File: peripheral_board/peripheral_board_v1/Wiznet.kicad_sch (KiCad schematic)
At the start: 27 parts, among them U4 W5500, Y2 25MHZ

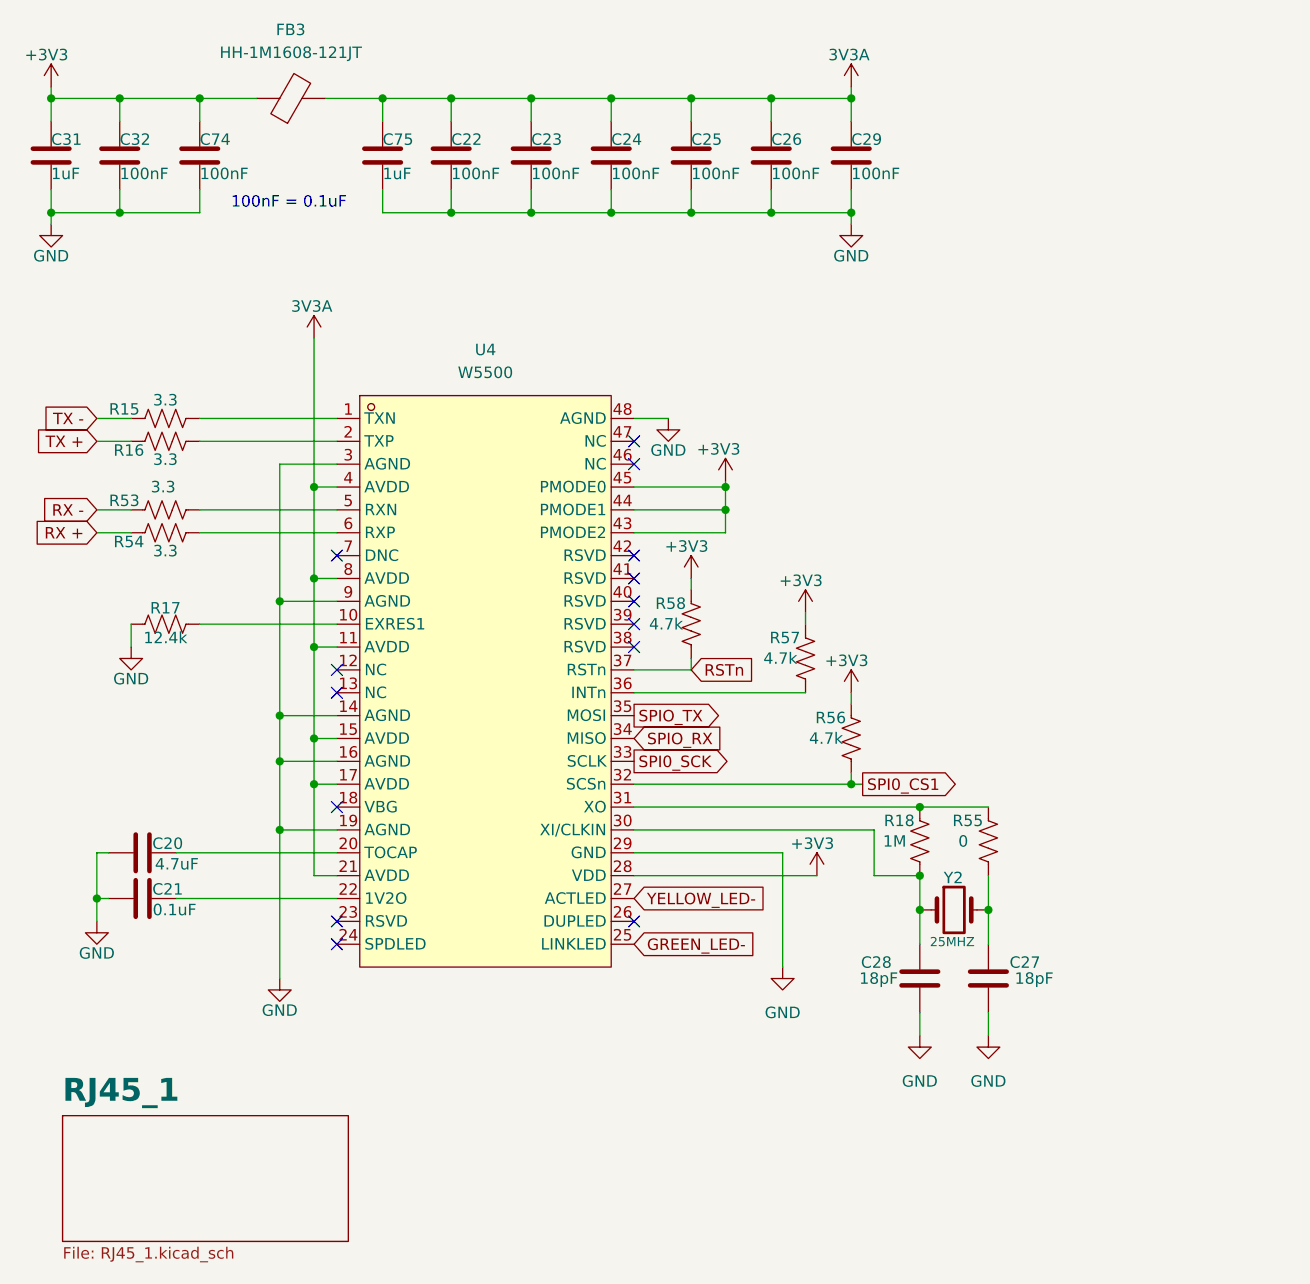
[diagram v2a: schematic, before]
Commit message: Update to the PCB
#Changes made so far

## Wiznet
* Changed the Wiznet layout to match that of their development board
* Restructured the RJ45 connections
    * *Looked over the RJ45 still a unsure*
    * Added in 2 differnt versions of Ethernt Connections. The one that shows the magnetics might be used for the Ethernet switch.
* Removed the Single Bus Buffer gate with 3-state output to match the dev board

## Raspberry Pi
* Moved to USB type C from micro USB for debugging.
* Changed the GPIO pins to match the Wiznet dev board.
* Brought in breakout pins for the rest of the GPIO.
* Cleaned up the Schematic to make it more clean.

## Ethernet Switch
* Changed the crystal to be the same as the Wiznet and to have the correct load caps
* Looking at the design check list to help get moving forward, need to relook at power distribution.
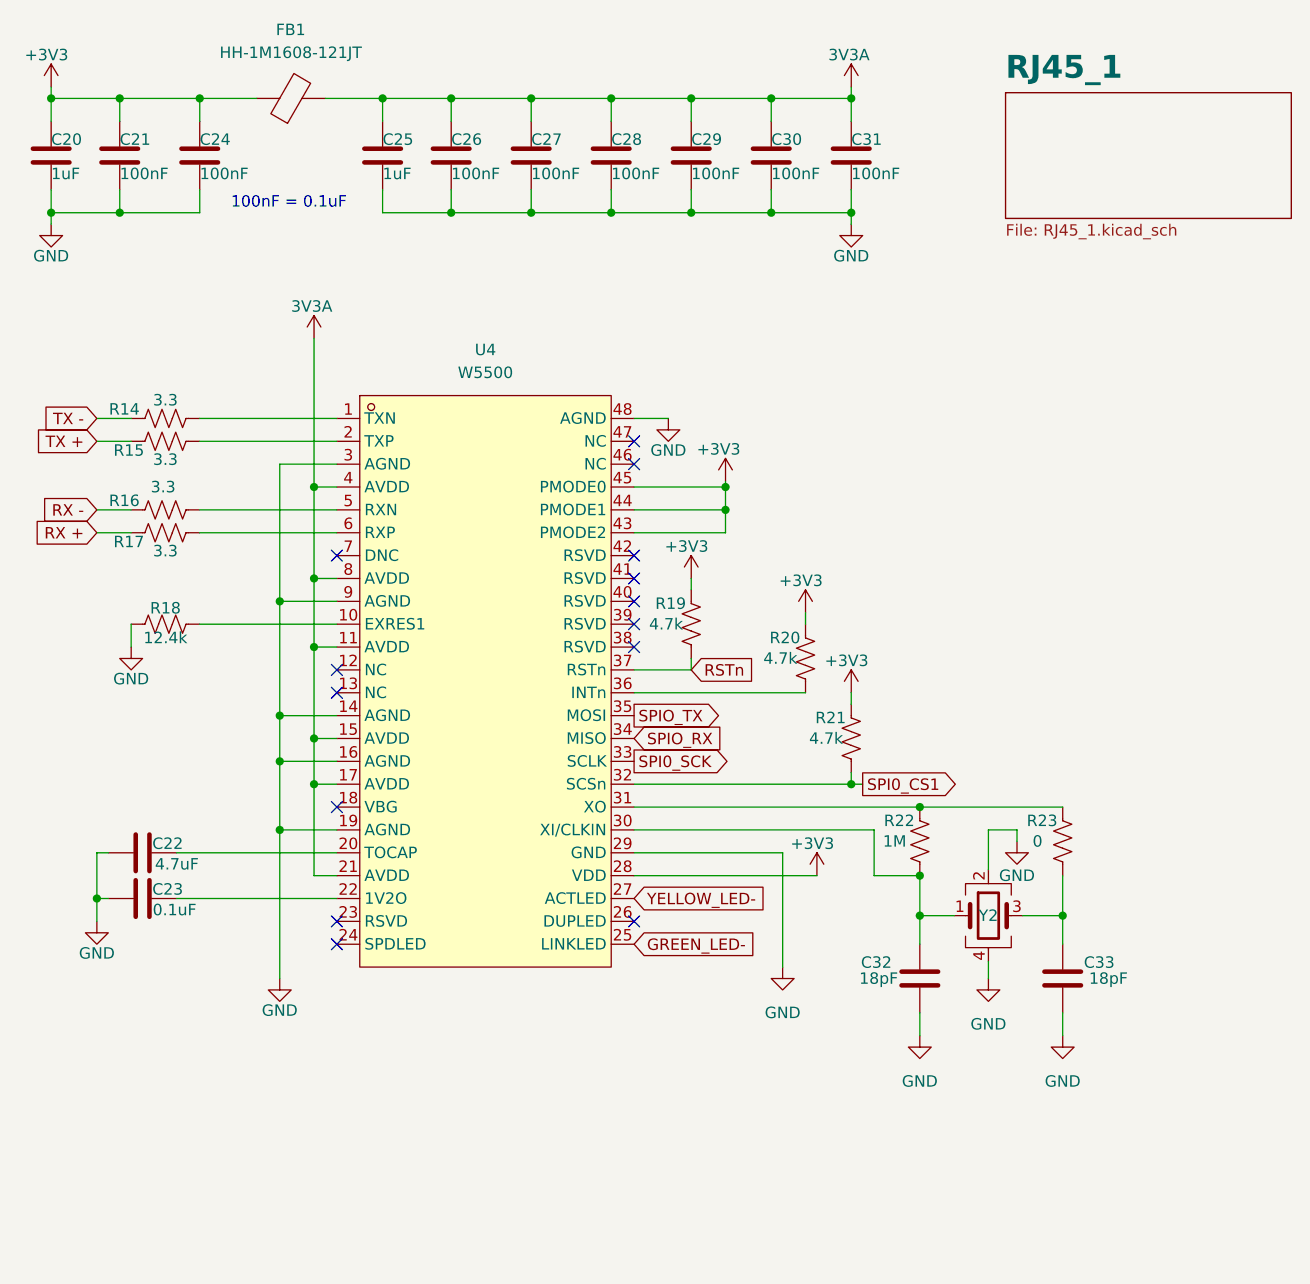
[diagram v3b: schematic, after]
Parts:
- removed Y2: 25MHZ, Crystal:Crystal_SMD_3225-4Pin_3.2x2.5mm, symbol Device:Crystal
- added Y2: ABMM-25.000MHZ-B2-T, Crystal:Crystal_SMD_7050-4Pin_7.0x5.0mm, symbol Device:Crystal_GND24
- renumbered C31 to C20, C32 to C21, C20 to C22, C21 to C23, C74 to C24, C75 to C25, C22 to C26, C23 to C27, C24 to C28, C25 to C29, C26 to C30, C29 to C31, C28 to C32, C27 to C33, FB3 to FB1, R15 to R14, R16 to R15, R53 to R16, R54 to R17, R17 to R18, R58 to R19, R57 to R20, R56 to R21, R18 to R22, R55 to R23
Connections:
- net GND: now also Y2.2, Y2.4
- net at C33.2, R23.1: now also Y2.3
- net at C32.2, R22.1, U4.30 (XI/CLKIN): now also Y2.1
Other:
- moved on the sheet: C33, R23

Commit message: Updated to the schematic
Kicad died on me so I needed to readd all my libraries to the project.

Added in the the Power board connector but want to go over it to make sure it will be implemented correctly. It is currently excluded.

Looked through the SALAD board and I had the same layout but I guess I did something wrong with selection of and or placement of signals traces. Added back in the single bus buffer, jumpers for changing the pmode and the filtering of the power and ground. It is currently excluded. Wiznet RJ45 connection is done.

Still going through the ethernet switch but found more info on the strap in mode. It is configured from the LED signals. The design guide has some specific details for the RJ45 and the Wiznet's RJ45 should be fine to use but I a Pulse JXD6-0001NL as a an easier stand in to better match the hardware design guideline. Still need to figure out the stand alone 4 port switch.
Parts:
- added FB4, FB5: FerriteBead, symbol Device:FerriteBead
- added JP1, JP2, JP3: SolderJumper_2_Open, symbol Jumper:SolderJumper_2_Open
- added RN?: 10k, Resistor_SMD:R_Array_Concave_4x0603, symbol Device:R_Pack04
- added U?: SN74AHC1G125DBVR, SCALES:SOT-23-5_L3.0-W1.7-P0.95-LS2.8-BR, symbol SCALES:SN74AHC1G125DBVR
- Y2: value ABMM-25.000MHZ-B2-T -> 25MHz; Type (none) -> ABMM-25.000MHZ-B2-T
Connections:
- net +3V3: now also FB4.1, RN?.5 (R4.2), RN?.6 (R3.2), RN?.7 (R2.2), RN?.8 (R1.2), U?.5 (VCC)
- net GND: now also FB5.1, JP1.2 (B), JP2.2 (B), JP3.2 (B), U?.3 (GND)
- net SPIO_RX: now also U?.2 (A)
- new net +3V3A: FB4.2
- new net GNDA: FB5.2
- new net INTN: RN?.4 (R4.1)
- new net PMODE0: JP1.1 (A), RN?.1 (R1.1)
- new net PMODE1: JP2.1 (A), RN?.2 (R2.1)
- new net PMODE2: JP3.1 (A), RN?.3 (R3.1)
- new net SPI0_MIS0: U?.4 (Y)
- new net SPIO_CS1: U?.1 (OE)
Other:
- note added: "Change to dip switch"
- note added: "This is from old proves and salad"

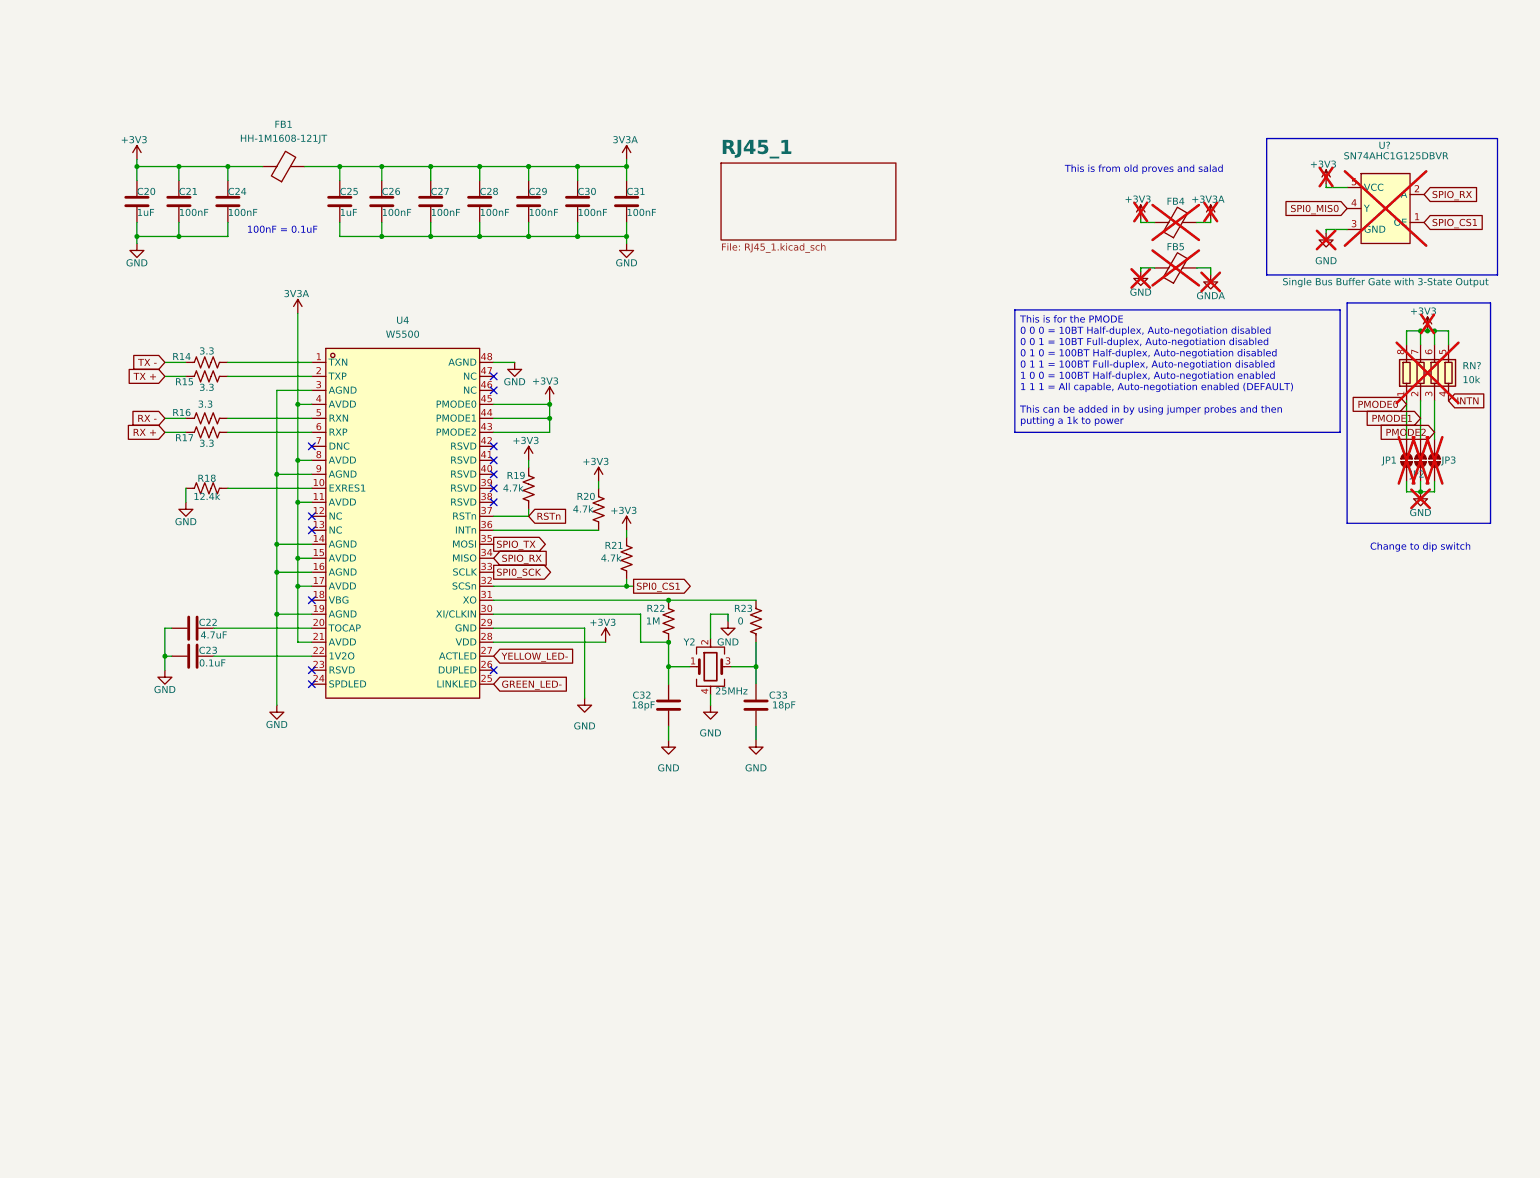
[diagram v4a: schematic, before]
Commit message: Schematic design ready for review
Made the last changes for the Wiznet by adding in Dip switches and made sure that the interrupt and reset signals are attached to the raspberry pi.

Finished the Etherent switch by wiring the RJ45 port 1 with 2 configurations, leaning more towards not using the Wiznet port but might do it any ways for cost. Added test points to port 5 but might change it to be RMII configuration because the 4 port strap in mode sets it to that config. Put solder jumpers in for the LED strap in mode. On the schematic I put in a note about how to configure to the proper mode we want but after a review will change to be a hardwire set. Made the reset switch match that of the EVAL board but further reading found I do not need the diode. Created the VDDIO and VDDAT which are just 2 different versions of 3.3V. Layout would be next but need to learn more about trace integrity and impedance control.
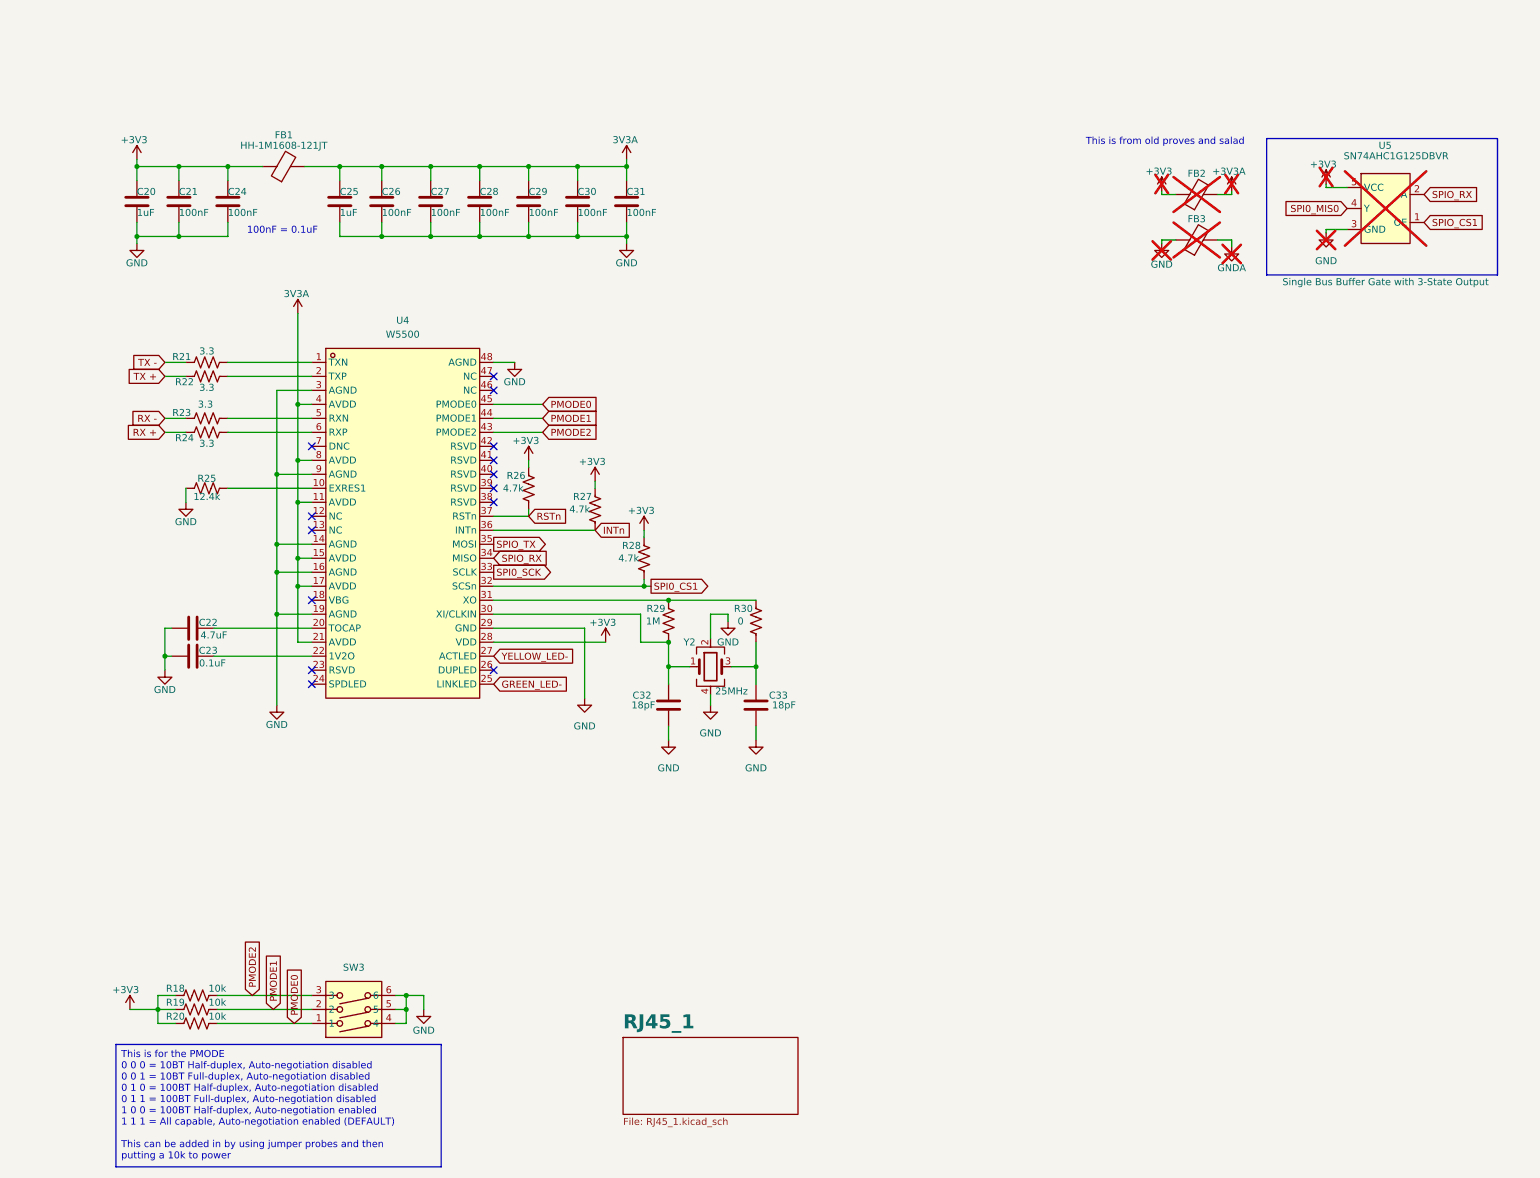
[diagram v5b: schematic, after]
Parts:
- removed JP1, JP2, JP3: SolderJumper_2_Open, symbol Jumper:SolderJumper_2_Open
- removed RN?: 10k, Resistor_SMD:R_Array_Concave_4x0603, symbol Device:R_Pack04
- added R18, R19, R20: 10k, Resistor_SMD:R_0603_1608Metric, symbol Device:R_US
- added SW3: 3_Pin_Dip_Switch_DSWB03LHGET_C25503178, SCALES:SW-TH_DSWB03LHGET, symbol SCALES:3_Pin_Dip_Switch_DSWB03LHGET_C25503178
- gave numbers to parts that had none: 1
- renumbered FB4 to FB2, FB5 to FB3, R14 to R21, R15 to R22, R16 to R23, R17 to R24, R18 to R25, R19 to R26, R20 to R27, R21 to R28, R22 to R29, R23 to R30
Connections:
- net +3V3: now also R18.2, R19.2, R20.2; no longer U4.43 (PMODE2), U4.44 (PMODE1), U4.45 (PMODE0)
- net GND: now also SW3.4, SW3.5, SW3.6
- net PMODE0: now also U4.45 (PMODE0), R20.1, SW3.1
- net PMODE1: now also U4.44 (PMODE1), R19.1, SW3.2
- net PMODE2: now also U4.43 (PMODE2), R18.1, SW3.3
- net INTn: now reaches R27.1, U4.36 (INTn)
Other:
- note removed: "Change to dip switch"
- moved on the sheet: FB2, FB3, R27, R28
